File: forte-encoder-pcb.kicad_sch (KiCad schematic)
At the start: 59 parts, among them CN3(OUT)1 XT30(2+2)PB-M.G.B, J0 BM07B-SRSS-TB(LF)(SN), J1 Conn_01x01_Pin, J10 Conn_01x01_Pin, J2 Conn_01x01_Pin, J3 Conn_01x01_Pin, J4 Conn_01x01_Pin, J5 Conn_01x01_Pin, J6 Conn_01x01_Pin, J7 Conn_01x01_Pin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

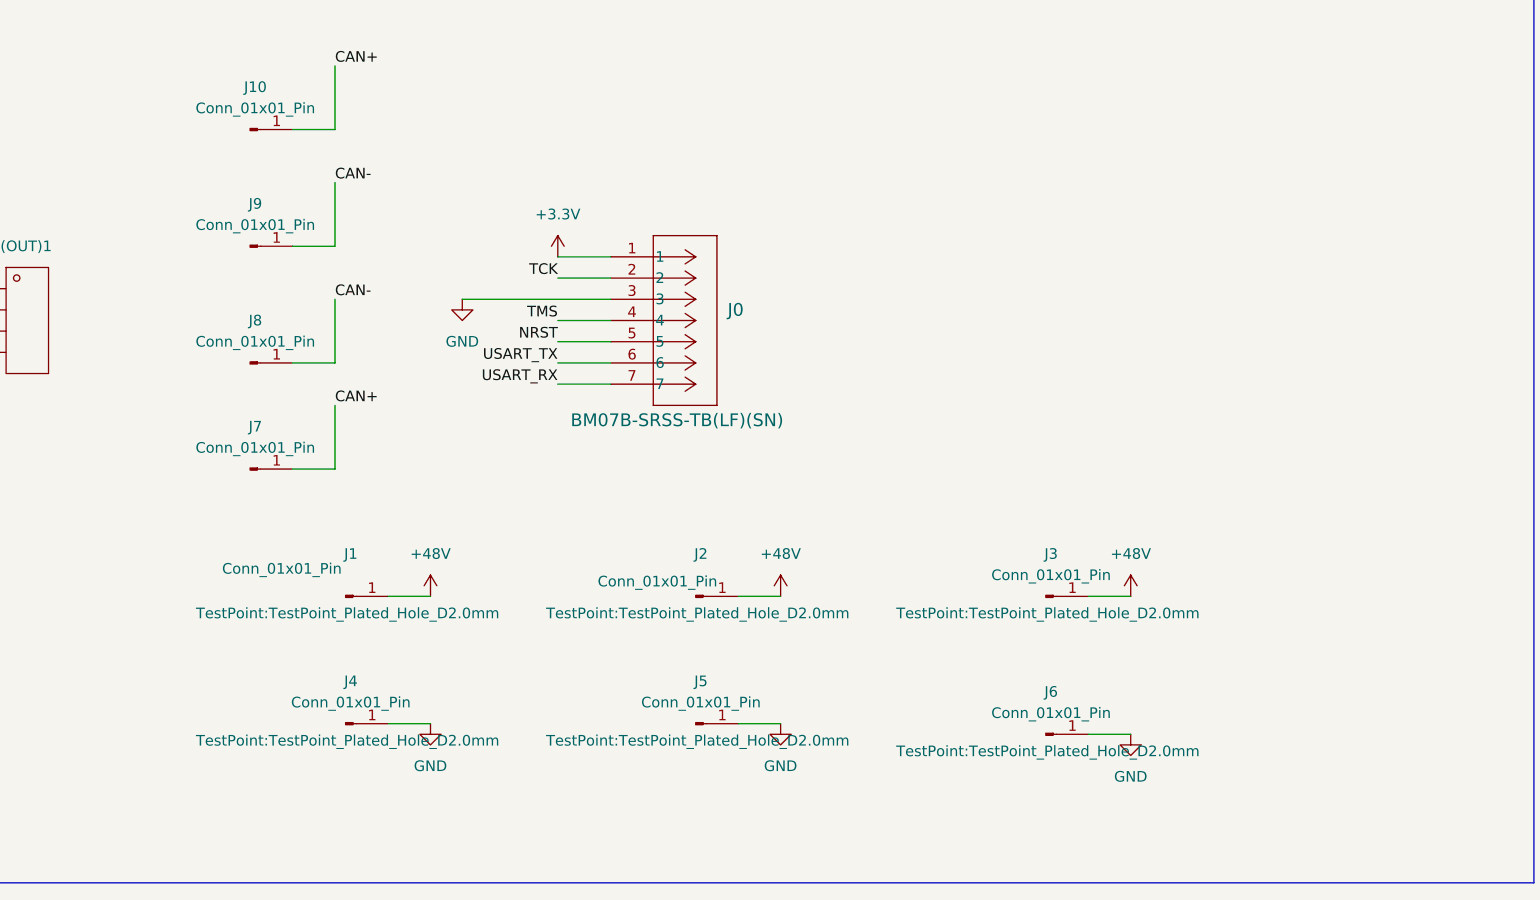
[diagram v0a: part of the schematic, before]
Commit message: rearange pcb
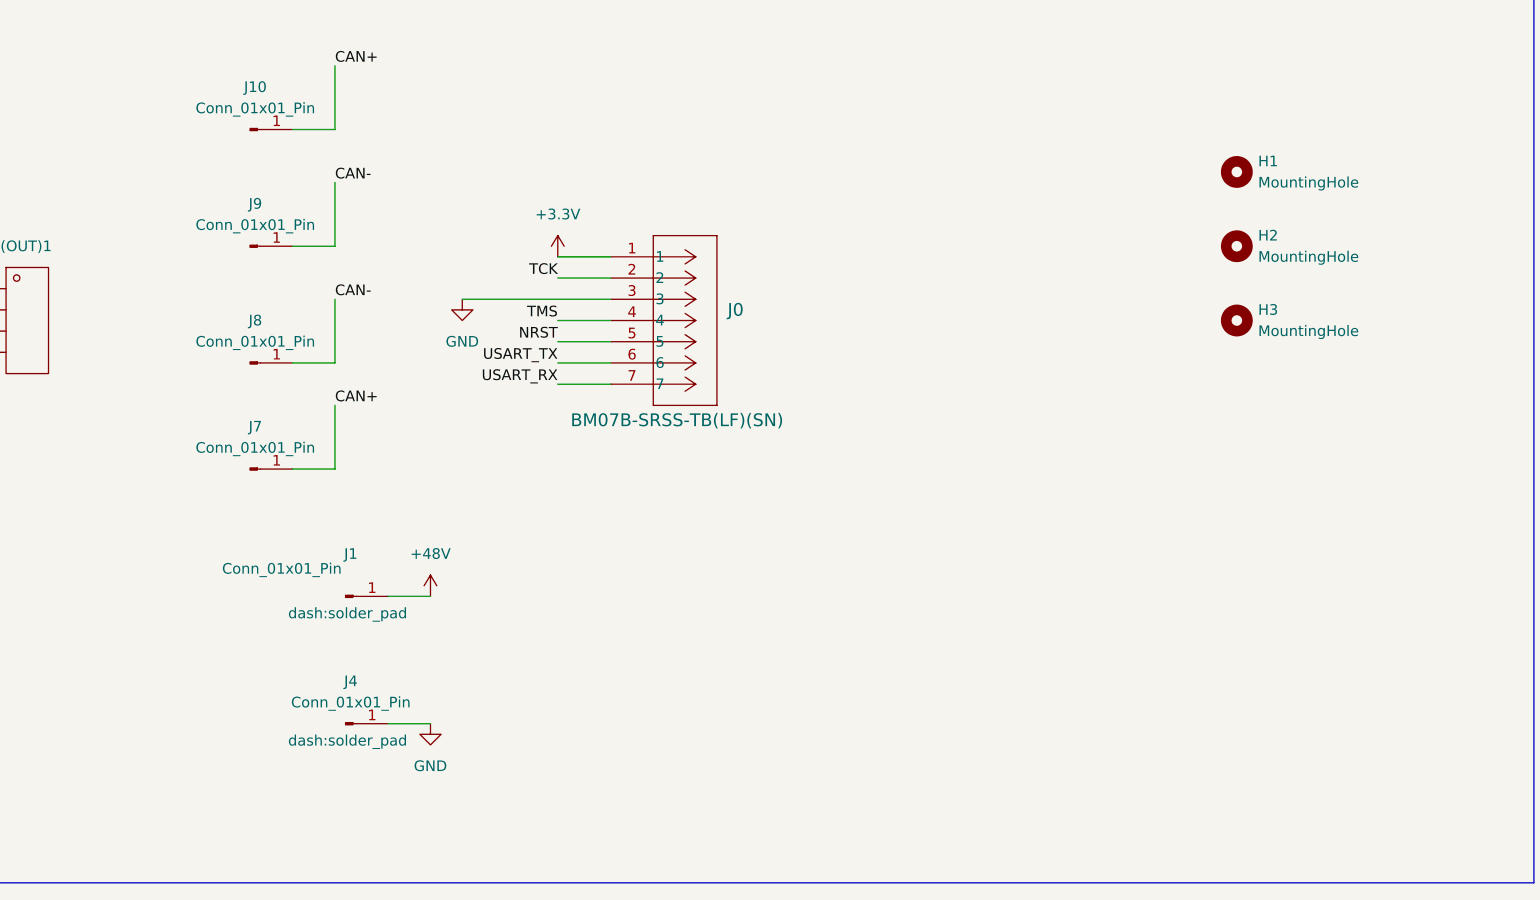
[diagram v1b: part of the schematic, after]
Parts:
- removed J2, J3, J5, J6: Conn_01x01_Pin, TestPoint:TestPoint_Plated_Hole_D2.0mm, symbol Connector:Conn_01x01_Pin
- added H1, H2, H3: MountingHole, MountingHole:MountingHole_2.1mm, symbol Mechanical:MountingHole
- J1, J4: footprint TestPoint:TestPoint_Plated_Hole_D2.0mm -> dash:solder_pad

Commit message: again
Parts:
- removed TP1: +12V TestPoint, TestPoint:TestPoint_THTPad_D1.5mm_Drill0.7mm, symbol Connector:TestPoint
- removed TP3: +5V TestPoint, TestPoint:TestPoint_THTPad_D1.5mm_Drill0.7mm, symbol Connector:TestPoint
- removed TP4: +3.3V TestPoint, TestPoint:TestPoint_THTPad_D1.5mm_Drill0.7mm, symbol Connector:TestPoint
- removed TP_GND2: GND TestPoint, TestPoint:TestPoint_THTPad_D1.5mm_Drill0.7mm, symbol Connector:TestPoint

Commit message: change port and rearange
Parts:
- removed J0: BM07B-SRSS-TB(LF)(SN), dash:BM07B-SRSS-TB, symbol dash:BM07B-SRSS-TB
- added J2: BM07B-GHS-TBT, dash:JST_BM07B-GHS-TBT, symbol dash:BM07B-GHS-TBT
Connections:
- net +3.3V: now also J2.1
- net GND: now also J2.3
- net NRST: now also J2.5
- net TCK: now also J2.2
- net TMS: now also J2.4
- net USART_RX: now also J2.7
- net USART_TX: now also J2.6
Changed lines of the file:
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@@
 	)
 	(symbol
+		(lib_id "dash:BM07B-GHS-TBT")
+		(at 495.3 160.02 0)
+		(unit 1)
+		(body_style 1)
+		(exclude_from_sim no)
+		(in_bom yes)
+		(on_board yes)
+		(in_pos_files yes)
+		(dnp no)
+		(fields_autoplaced yes)
+		(property "Reference" "J2"
+			(at 501.65 158.7499 0)
+			(show_name no)
+			(do_not_autoplace no)
+			(effects
+				(font
+					(size 1.27 1.27)
+				)
+				(justify left)
+			)
+		)
+		(property "Value" "BM07B-GHS-TBT"
+			(at 501.65 161.2899 0)
+			(show_name no)
+			(do_not_autoplace no)
+			(effects
+				(font
+					(size 1.27 1.27)
+				)
+				(justify left)
+			)
+		)
+		(property "Footprint" "dash:JST_BM07B-GHS-TBT"
+			(at 495.3 160.02 0)
+			(hide yes)
+			(show_name no)
+			(do_not_autoplace no)
+			(effects
+				(font
+					(size 1.27 1.27)
+				)
+				(justify bottom)
+			)
+		)
+		(property "Datasheet" ""
+			(at 495.3 160.02 0)
+			(hide yes)
+			(show_name no)
+			(do_not_autoplace no)
+			(effects
+				(font
+					(size 1.27 1.27)
+				)
+			)
+		)
+		(property "Description" ""
+			(at 495.3 160.02 0)
+			(hide yes)
+			(show_name no)
+			(do_not_autoplace no)
+			(effects
+				(font
+					(size 1.27 1.27)
+				)
+			)
+		)
+		(property "PARTREV" "NA"
+			(at 495.3 160.02 0)
+			(hide yes)
+			(show_name no)
+			(do_not_autoplace no)
+			(effects
+				(font
+					(size 1.27 1.27)
+				)
+				(justify bottom)
+			)
+		)
+		(property "STANDARD" "Manufacturer Recommendations"
+			(at 495.3 160.02 0)
+			(hide yes)
+			(show_name no)
+			(do_not_autoplace no)
+			(effects
+				(font
+					(size 1.27 1.27)
+				)
+				(justify bottom)
+			)
+		)
+		(property "MAXIMUM_PACKAGE_HEIGHT" "4.2mm"
+			(at 495.3 160.02 0)
+			(hide yes)
+			(show_name no)
+			(do_not_autoplace no)
+			(effects
+				(font
+					(size 1.27 1.27)
+				)
+				(justify bottom)
+			)
+		)
+		(property "MANUFACTURER" "JST"
+			(at 495.3 160.02 0)
+			(hide yes)
+			(show_name no)
+			(do_not_autoplace no)
+			(effects
+				(font
+					(size 1.27 1.27)
+				)
+				(justify bottom)
+			)
+		)
+		(pin "6"
+		)
+		(pin "7"
+		)
+		(pin "5"
+		)
+		(pin "4"
+		)
+		(pin "3"
+		)
+		(pin "2"
+		)
+		(pin "1"
+		)
+		(instances
+			(project "forte-encoder-pcb"
+				(path "/4fd4f7f7-4e27-480c-b1ee-dc0730be04ca"
+					(reference "J2")
+					(unit 1)
+				)
+			)
+		)
+	)
+	(symbol
 		(lib_id "power:+12V")
 		(at 655.32 50.8 90)
@@
 					(unit 1)
 				)
-			)
-		)
-	)
-	(symbol
-		(lib_id "dash:BM07B-SRSS-TB")
-		(at 487.68 152.4 0)
-		(unit 1)
-		(body_style 1)
-		(exclude_from_sim no)
-		(in_bom yes)
-		(on_board yes)
-		(in_pos_files yes)
-		(dnp no)
-		(property "Reference" "J0"
-			(at 501.65 158.7499 0)
-			(show_name no)
-			(do_not_autoplace no)
-			(effects
-				(font
-					(size 1.524 1.524)
-				)
-				(justify left)
-			)
-		)
-		(property "Value" "BM07B-SRSS-TB(LF)(SN)"
-			(at 482.854 171.958 0)
-			(show_name no)
-			(do_not_autoplace no)
-			(effects
-				(font
-					(size 1.524 1.524)
-				)
-				(justify left)
-			)
-		)
-		(property "Footprint" "dash:BM07B-SRSS-TB"
-			(at 487.68 152.4 0)
-			(hide yes)
-			(show_name no)
-			(do_not_autoplace no)
-			(effects
-				(font
-					(size 1.27 1.27)
-					(italic yes)
-				)
-			)
-		)
-		(property "Datasheet" "BM07B-SRSS-TB"
-			(at 487.68 152.4 0)
-			(hide yes)
-			(show_name no)
-			(do_not_autoplace no)
-			(effects
-				(font
-					(size 1.27 1.27)
-					(italic yes)
-				)
-			)
-		)
-		(property "Description" ""
-			(at 487.68 152.4 0)
-			(hide yes)
-			(show_name no)
-			(do_not_autoplace no)
-			(effects
-				(font
-					(size 1.27 1.27)
-				)
-			)
-		)
-		(pin "5"
-		)
-		(pin "3"
-		)
-		(pin "7"
-		)
-		(pin "2"
-		)
-		(pin "6"
-		)
-		(pin "4"
-		)
-		(pin "1"
-		)
-		(instances
-			(project "forte-encoder-pcb"
-				(path "/4fd4f7f7-4e27-480c-b1ee-dc0730be04ca"
-					(reference "J0")
-					(unit 1)
-				)
